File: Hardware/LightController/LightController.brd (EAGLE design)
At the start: 71.1 x 70 mm, 28 parts, among them IC1 ATMEGA328P, K1 G5LE, Q1 8MHz, Q2 2N3704, X1 IN, X2 OUT, X3 EARTH

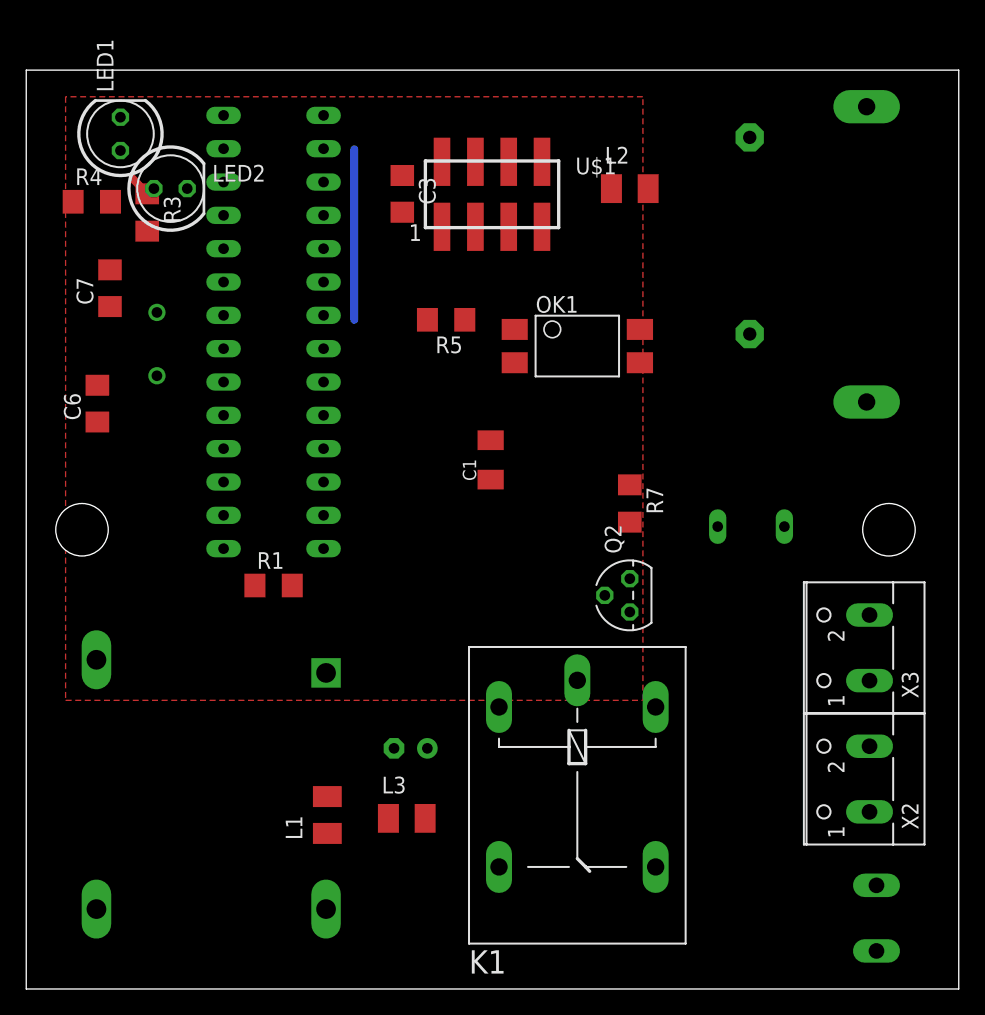
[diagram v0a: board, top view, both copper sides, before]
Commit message: updated incorrect outer dimension
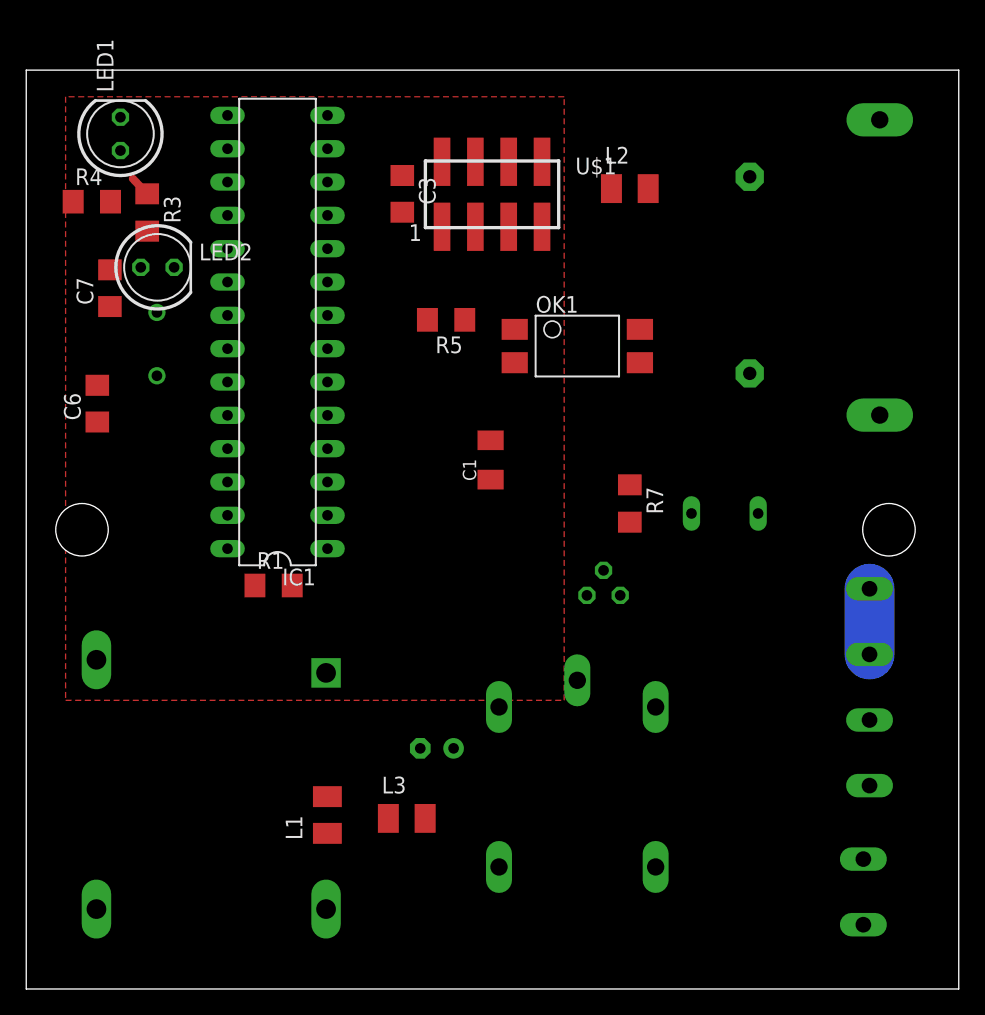
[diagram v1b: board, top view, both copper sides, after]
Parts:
- moved LED2 6.08 mm to (10.0, 55.0)
- moved C5 3.00 mm to (55.1, 54.4)
- moved R2 2.24 mm to (53.2, 36.2)
- moved X1 2.24 mm to (62.5, 7.40)
- moved C4 2.00 mm to (31.3, 18.3)
- moved Q2 2.00 mm to (44.0, 30.0), flipped to the bottom, turned to 0 degrees
- moved X2 2.00 mm to (63.0, 18.0), flipped to the bottom, turned to 270 degrees
- moved X3 2.00 mm to (63.0, 28.0), flipped to the bottom, turned to 270 degrees
- moved F1 1.41 mm to (65.0, 55.0)
- moved IC1 0.30 mm to (19.1, 50.1), flipped to the top
- flipped K1 to the bottom
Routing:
- net +3V3: track 13.0 -> 0.00 mm
- net N$14: track 0.00 -> 5.00 mm

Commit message: updated processoor to be surface mount. created intial route for pcb tracks. Had to use dual layer board to allow for small form factor
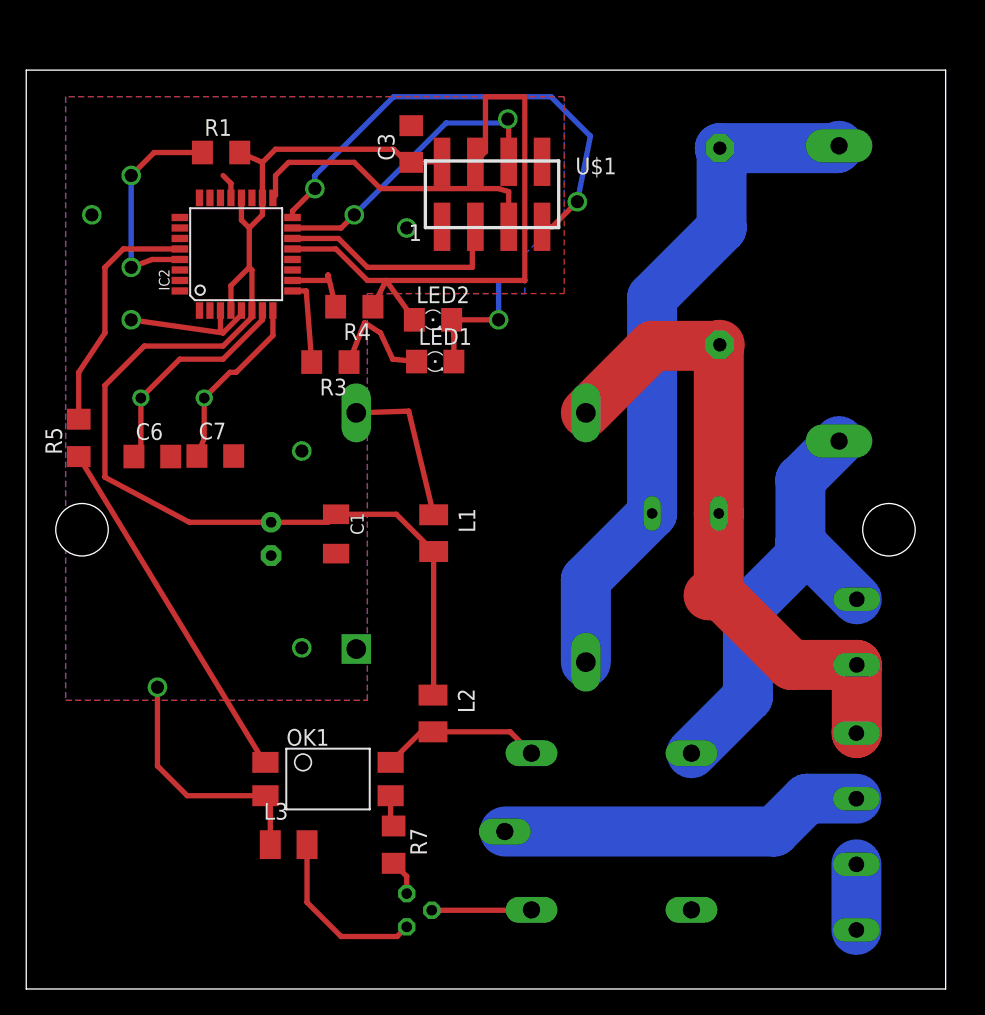
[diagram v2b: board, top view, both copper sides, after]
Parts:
- removed IC1: ATMEGA328P, ic-package:DIL28-3
- added IC2: ATMEGA328P-AU, ATMEGA328P:TQFP32-08
- LED1, LED2: device led:LED5MM -> led:1206
- moved L2 42.7 mm to (31.0, 21.0), turned to 270 degrees
- moved OK1 38.1 mm to (23.0, 16.0)
- moved R1 33.2 mm to (14.8, 63.8)
- moved R7 31.6 mm to (28.0, 11.0)
- moved LED1 29.6 mm to (31.2, 47.8), turned to 0 degrees
- moved R5 29.4 mm to (4.00, 42.0), turned to 90 degrees
- moved Q2 28.3 mm to (29.0, 6.00), turned to 90 degrees
- moved U$2 27.3 mm to (33.9, 34.4), turned to 0 degrees
- moved L1 23.0 mm to (31.1, 34.7), turned to 270 degrees
- moved R4 21.5 mm to (25.0, 52.0), turned to 180 degrees
- moved LED2 21.4 mm to (31.0, 51.0)
- moved X3 21.0 mm to (62.0, 7.00)
- moved C4 20.4 mm to (18.7, 34.3), turned to 270 degrees
- moved X1 19.8 mm to (62.0, 27.2)
- moved R3 18.0 mm to (23.2, 47.8), turned to 180 degrees
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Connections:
- removed net N$10: IC1.12, R4.2
- new net N$19: IC2.9, R3.2
- net +3V3: now also IC2.18, IC2.20, IC2.4, IC2.6; no longer IC1.20, IC1.21, IC1.7
- net CE_RAD: now also IC2.14; no longer IC1.16
- net CSN_RAD: now also IC2.13; no longer IC1.15
- net GND: now also IC2.21, IC2.3, IC2.5, LED1.C, LED2.C; no longer IC1.22, IC1.8, LED1.K, LED2.K
- net MISO: now also IC2.16; no longer IC1.18
- net MOSI: now also IC2.15; no longer IC1.17
- net N$1: now also K1.S; no longer K1.P
- net N$13: now also K1.P, X2.2; no longer K1.S, X2.1
- net N$3: now also IC2.29; no longer IC1.1
- net N$4: now also X2.1; no longer X2.2
- net N$5: now also IC2.10, R4.2; no longer IC1.11, R3.2
- net N$7: now also IC2.28; no longer IC1.28
- net N$8: now also IC2.7; no longer IC1.9
- net N$9: now also IC2.8; no longer IC1.10
- net SCK: now also IC2.17; no longer IC1.19
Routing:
- net +3V3: track 0.00 -> 93.7 mm
- net N$2: track 0.00 -> 52.7 mm
- net N$4: track 0.00 -> 50.2 mm
- net GND: track 0.00 -> 41.9 mm, vias 0 -> 7
- net CSN_RAD: track 0.00 -> 41.3 mm
- net MISO: track 0.00 -> 37.2 mm, vias 0 -> 2
- net N$1: track 0.00 -> 34.5 mm
- net N$13: track 0.00 -> 27.8 mm
- net N$12: track 0.00 -> 27.3 mm
- net SCK: track 0.00 -> 23.5 mm
- net MOSI: track 0.00 -> 23.1 mm, vias 0 -> 2
- net N$7: track 0.00 -> 18.5 mm
- net CE_RAD: track 0.00 -> 17.8 mm
- net N$8: track 0.00 -> 17.1 mm
- net N$3: track 0.00 -> 17.0 mm, vias 0 -> 2
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- added copper zone on layer 16, net GND
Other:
- board size 71.1 x 70 mm -> 70.1 x 70 mm

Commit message: added flyback diode and tidied traces
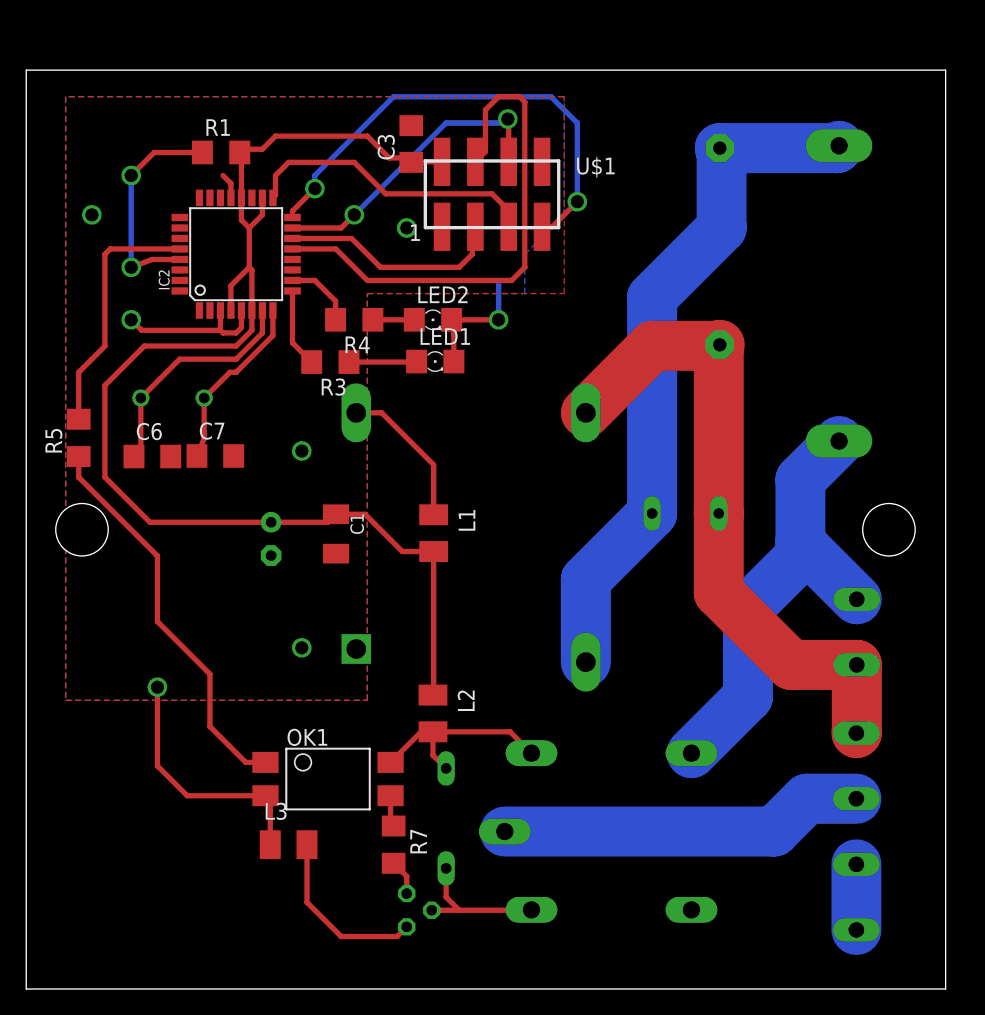
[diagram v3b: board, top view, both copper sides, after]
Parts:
- added D1: 1N4148DO35-7, diode:DO35-7
- moved R4 1.00 mm to (25.0, 51.0)
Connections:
- net N$16: now also D1.A
- net VCC: now also D1.C
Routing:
- net N$16: track 7.61 -> 11.2 mm
- net N$6: track 8.70 -> 5.16 mm
- net VCC: track 12.4 -> 15.6 mm
- net N$11: track 5.93 -> 3.16 mm
- net N$12: track 27.3 -> 30.1 mm
- net +3V3: track 93.7 -> 96.0 mm
- net CSN_RAD: track 41.3 -> 39.9 mm
- net N$4: track 50.2 -> 49.2 mm
- net GND: track 41.9 -> 42.9 mm
- net N$7: track 18.5 -> 19.3 mm
- net SCK: track 23.5 -> 22.7 mm
- net VOUT: track 12.1 -> 11.4 mm
- net N$8: track 17.1 -> 17.6 mm
- net CE_RAD: track 17.8 -> 17.2 mm
- net MISO: track 37.2 -> 36.7 mm
